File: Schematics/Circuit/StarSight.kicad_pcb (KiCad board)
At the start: 2 copper layers, 37 parts, among them IC1 LM2956-5V, J1 Conn_02x20_Odd_Even, J10 IR1, J11 IR1, J12 ultSound1, J13 ultSound1, J14 ultSound1, J15 ultSound1, J16 Conn_01x02, J17 Conn_01x03, J18 Conn_01x19, J19 Conn_01x04, J2 Line1, J20 Conn_01x09, J21 Conn_01x12, J22 Conn_01x08, J3 Line2, J4 Line3, J5 Line4, J6 Line5, J7 IR1, J8 IR1, J9 IR1, P2 Power, Q4 BUZZ TO220

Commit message: Edit circuit exports
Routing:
- net +5V: track 271.9 -> 306.4 mm
- net Net-(J18-Pad6): track 0.00 -> 3.30 mm

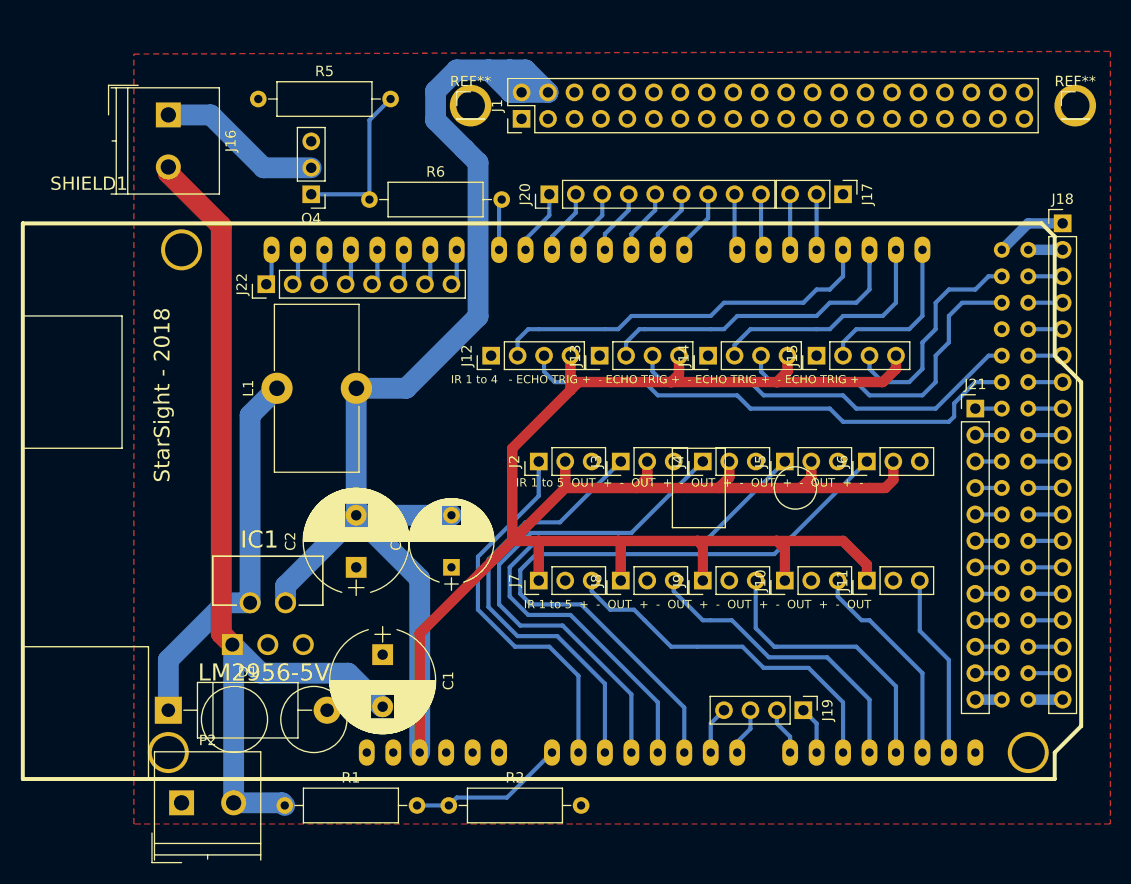
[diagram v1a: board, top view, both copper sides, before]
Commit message: Add pins for raspberry and few circuit fixes
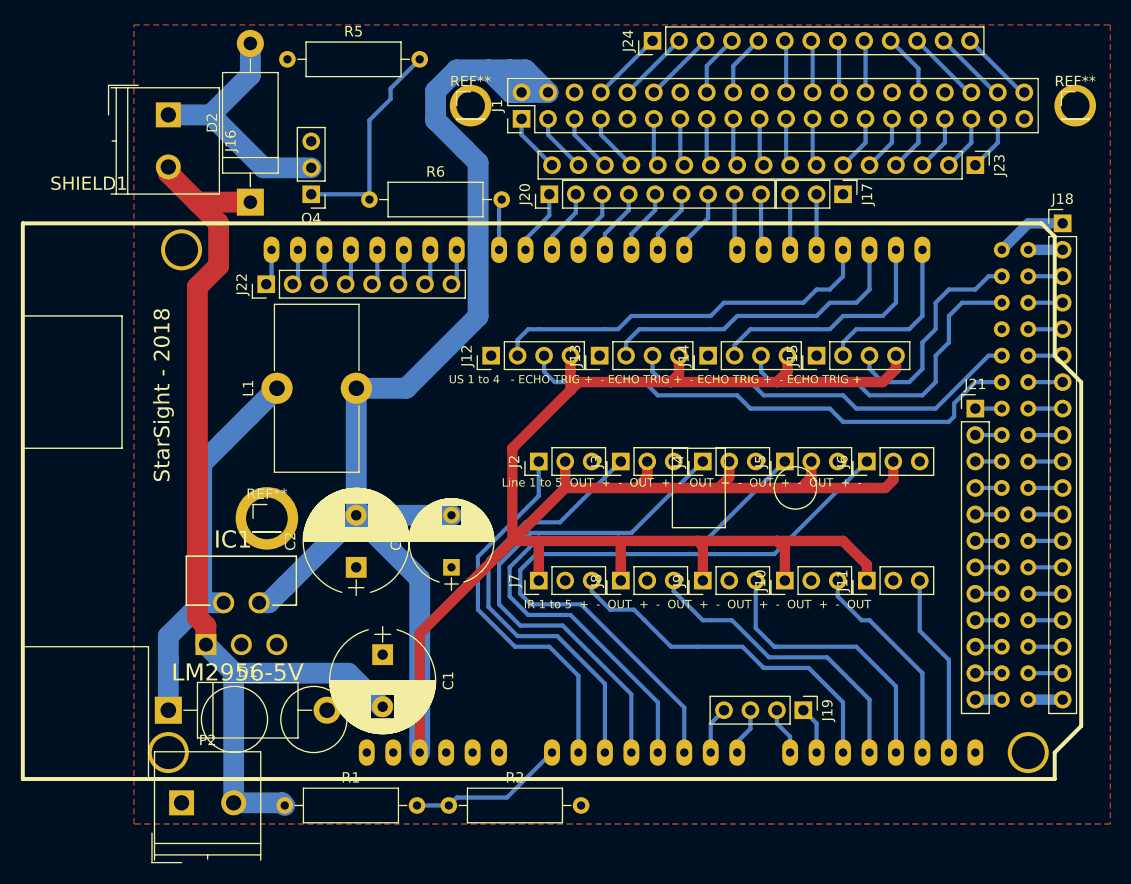
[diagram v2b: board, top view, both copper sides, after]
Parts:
- added D2: D, Diodes_THT:D_DO-201_P15.24mm_Horizontal, F.Cu at (124.7, 62.7)
- added J23: Conn_01x17, Pin_Headers:Pin_Header_Straight_1x17_Pitch2.54mm, F.Cu at (194.3, 59.2)
- added J24: Conn_01x13, Pin_Headers:Pin_Header_Straight_1x13_Pitch2.54mm, F.Cu at (163.3, 47.2)
- added REF**: Pin_Header_Straight_1x01_Pitch2.54mm, Pin_Headers:Pin_Header_Straight_1x01_Pitch2.54mm, F.Cu at (126.3, 93.1)
- moved R5 4.72 mm to (128.3, 49.0)
- moved IC1 2.54 mm to (127.3, 93.0)
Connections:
- J1 pad 1: (no net) -> Net-(J1-Pad1)
- J1 pad 10: (no net) -> Net-(J1-Pad10)
- J1 pad 11: (no net) -> Net-(J1-Pad11)
- J1 pad 12: (no net) -> Net-(J1-Pad12)
- J1 pad 13: (no net) -> Net-(J1-Pad13)
- J1 pad 15: (no net) -> Net-(J1-Pad15)
- J1 pad 16: (no net) -> Net-(J1-Pad16)
- J1 pad 17: (no net) -> Net-(J1-Pad17)
- J1 pad 18: (no net) -> Net-(J1-Pad18)
- J1 pad 19: (no net) -> Net-(J1-Pad19)
- J1 pad 21: (no net) -> Net-(J1-Pad21)
- J1 pad 22: (no net) -> Net-(J1-Pad22)
- J1 pad 23: (no net) -> Net-(J1-Pad23)
- J1 pad 24: (no net) -> Net-(J1-Pad24)
- J1 pad 26: (no net) -> Net-(J1-Pad26)
- J1 pad 27: (no net) -> Net-(J1-Pad27)
- J1 pad 28: (no net) -> Net-(J1-Pad28)
- J1 pad 29: (no net) -> Net-(J1-Pad29)
- J1 pad 3: (no net) -> Net-(J1-Pad3)
- J1 pad 31: (no net) -> Net-(J1-Pad31)
- J1 pad 32: (no net) -> Net-(J1-Pad32)
- J1 pad 33: (no net) -> Net-(J1-Pad33)
- J1 pad 35: (no net) -> Net-(J1-Pad35)
- J1 pad 36: (no net) -> Net-(J1-Pad36)
- J1 pad 37: (no net) -> Net-(J1-Pad37)
- J1 pad 38: (no net) -> Net-(J1-Pad38)
- J1 pad 40: (no net) -> Net-(J1-Pad40)
- J1 pad 5: (no net) -> Net-(J1-Pad5)
- J1 pad 7: (no net) -> Net-(J1-Pad7)
- J1 pad 8: (no net) -> Net-(J1-Pad8)
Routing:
- net Net-(D2-Pad2): track 15.8 -> 24.3 mm
- net Net-(J1-Pad40): track 0.00 -> 7.26 mm
- net Net-(J1-Pad38): track 0.00 -> 7.26 mm
- net Net-(J1-Pad36): track 0.00 -> 7.26 mm
- net Net-(J1-Pad8): track 0.00 -> 7.00 mm
- net Net-(J1-Pad10): track 0.00 -> 7.00 mm
- net Net-(J1-Pad12): track 0.00 -> 7.00 mm
- net Net-(J1-Pad32): track 0.00 -> 6.06 mm
- net Net-(J1-Pad18): track 0.00 -> 5.95 mm
- net Net-(J1-Pad16): track 0.00 -> 5.95 mm
- net Net-(J1-Pad3): track 0.00 -> 5.65 mm
- net Net-(J1-Pad7): track 0.00 -> 5.65 mm
- net Net-(J1-Pad5): track 0.00 -> 5.65 mm
- net Net-(J1-Pad1): track 0.00 -> 5.65 mm
- net +12V: track 85.5 -> 91.1 mm
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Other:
- board text added: "Line 1 to 5 OUT + - OUT + - OUT + - OUT + - OUT + -"
- board text added: "US 1 to 4 - ECHO TRIG + - ECHO TRIG + - ECHO TRIG + - ECHO TRIG +"
- board text removed: "IR 1 to 4 - ECHO TRIG + - ECHO TRIG + - ECHO TRIG + - ECHO TRIG +"
- board text removed: "IR 1 to 5 OUT + - OUT + - OUT + - OUT + - OUT + -"
